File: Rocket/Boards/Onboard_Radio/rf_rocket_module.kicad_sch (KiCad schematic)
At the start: 9 parts

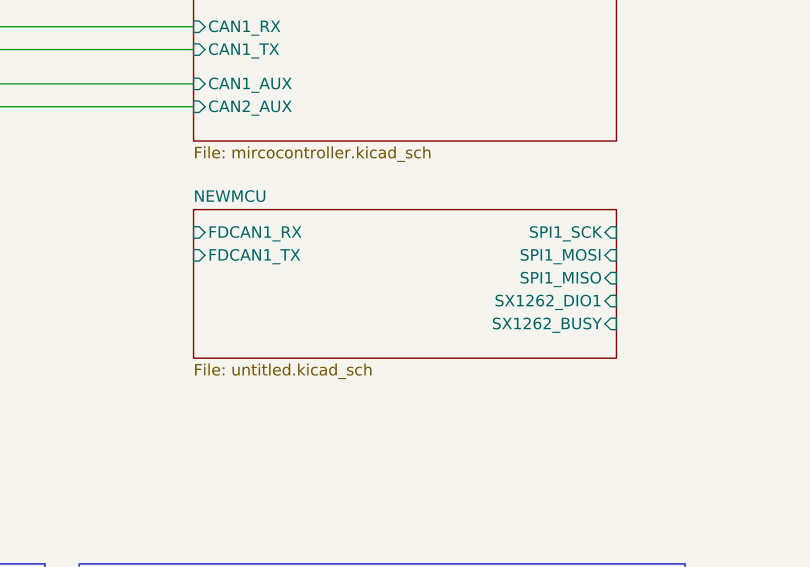
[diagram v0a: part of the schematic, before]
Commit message: python sim code added
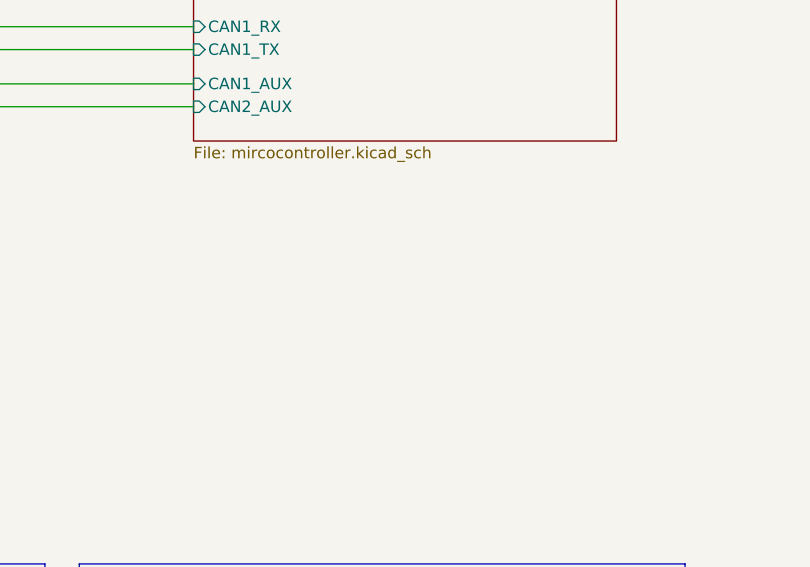
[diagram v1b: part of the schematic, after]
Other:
- removed sheet NEWMCU
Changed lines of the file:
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@@
-	)
-	(sheet
-		(at 77.47 102.87)
-		(size 46.99 16.51)
-		(exclude_from_sim no)
-		(in_bom yes)
-		(on_board yes)
-		(dnp no)
-		(fields_autoplaced yes)
-		(stroke
-			(width 0.1524)
-			(type solid)
-		)
-		(fill
-			(color 0 0 0 0.0000)
-		)
-		(property "Sheetname" "NEWMCU"
-			(at 77.47 102.1584 0)
-			(effects
-				(font
-					(size 1.27 1.27)
-				)
-				(justify left bottom)
-			)
-		)
-		(property "Sheetfile" "untitled.kicad_sch"
-			(at 77.47 119.9646 0)
-			(effects
-				(font
-					(size 1.27 1.27)
-				)
-				(justify left top)
-			)
-		)
-		(property "Field2" ""
-			(at 77.47 102.87 0)
-			(effects
-				(font
-					(size 1.27 1.27)
-				)
-			)
-		)
-		(property "Field3" ""
-			(at 77.47 102.87 0)
-			(effects
-				(font
-					(size 1.27 1.27)
-				)
-			)
-		)
-		(pin "FDCAN1_RX" input
-			(at 77.47 105.41 180)
-			(effects
-				(font
-					(size 1.27 1.27)
-				)
-				(justify left)
-			)
-		)
-		(pin "FDCAN1_TX" input
-			(at 77.47 107.95 180)
-			(effects
-				(font
-					(size 1.27 1.27)
-				)
-				(justify left)
-			)
-		)
-		(pin "SPI1_MISO" input
-			(at 124.46 110.49 0)
-			(effects
-				(font
-					(size 1.27 1.27)
-				)
-				(justify right)
-			)
-		)
-		(pin "SPI1_MOSI" input
-			(at 124.46 107.95 0)
-			(effects
-				(font
-					(size 1.27 1.27)
-				)
-				(justify right)
-			)
-		)
-		(pin "SPI1_SCK" input
-			(at 124.46 105.41 0)
-			(effects
-				(font
-					(size 1.27 1.27)
-				)
-				(justify right)
-			)
-		)
-		(pin "SX1262_BUSY" input
-			(at 124.46 115.57 0)
-			(effects
-				(font
-					(size 1.27 1.27)
-				)
-				(justify right)
-			)
-		)
-		(pin "SX1262_DIO1" input
-			(at 124.46 113.03 0)
-			(effects
-				(font
-					(size 1.27 1.27)
-				)
-				(justify right)
-			)
-		)
-		(instances
-			(project "rf_rocket_module"
-				(path "/4940ffbe-f45f-4917-a247-12e2b32b6c35"
-					(page "6")
-				)
-			)
-		)
 	)
 	(sheet

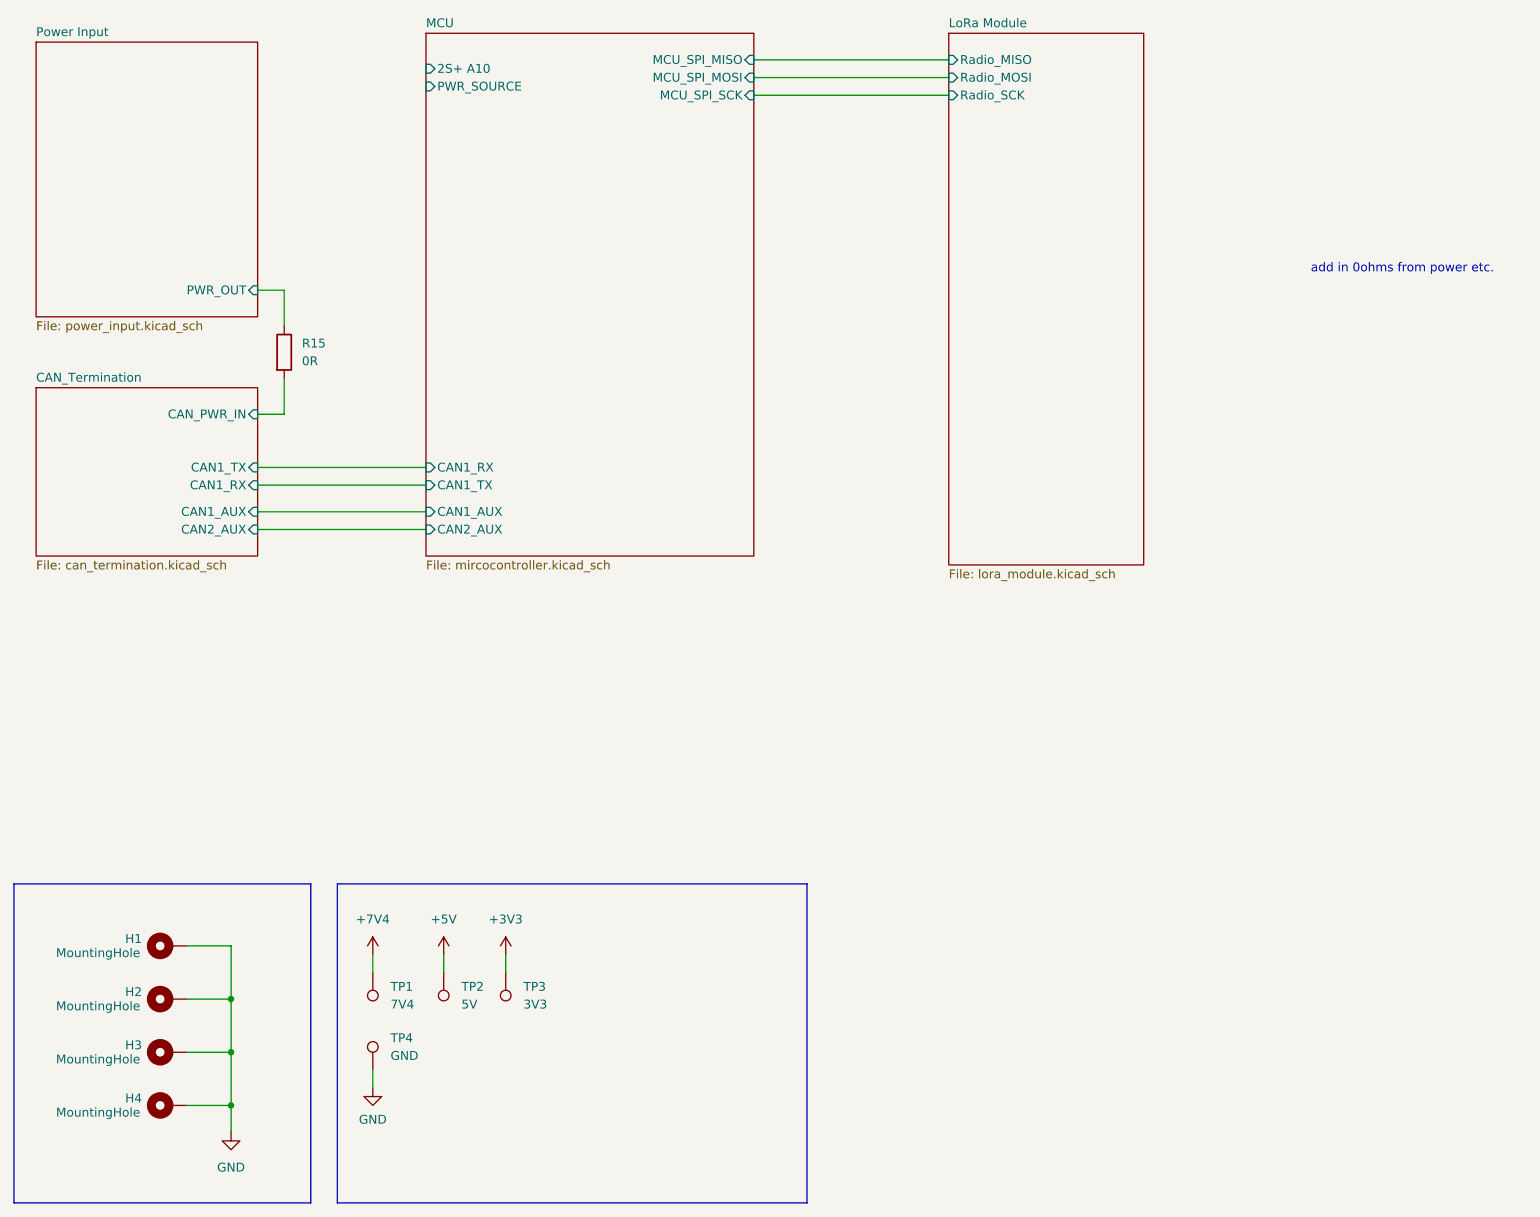
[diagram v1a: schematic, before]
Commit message: rf chip schematic changed
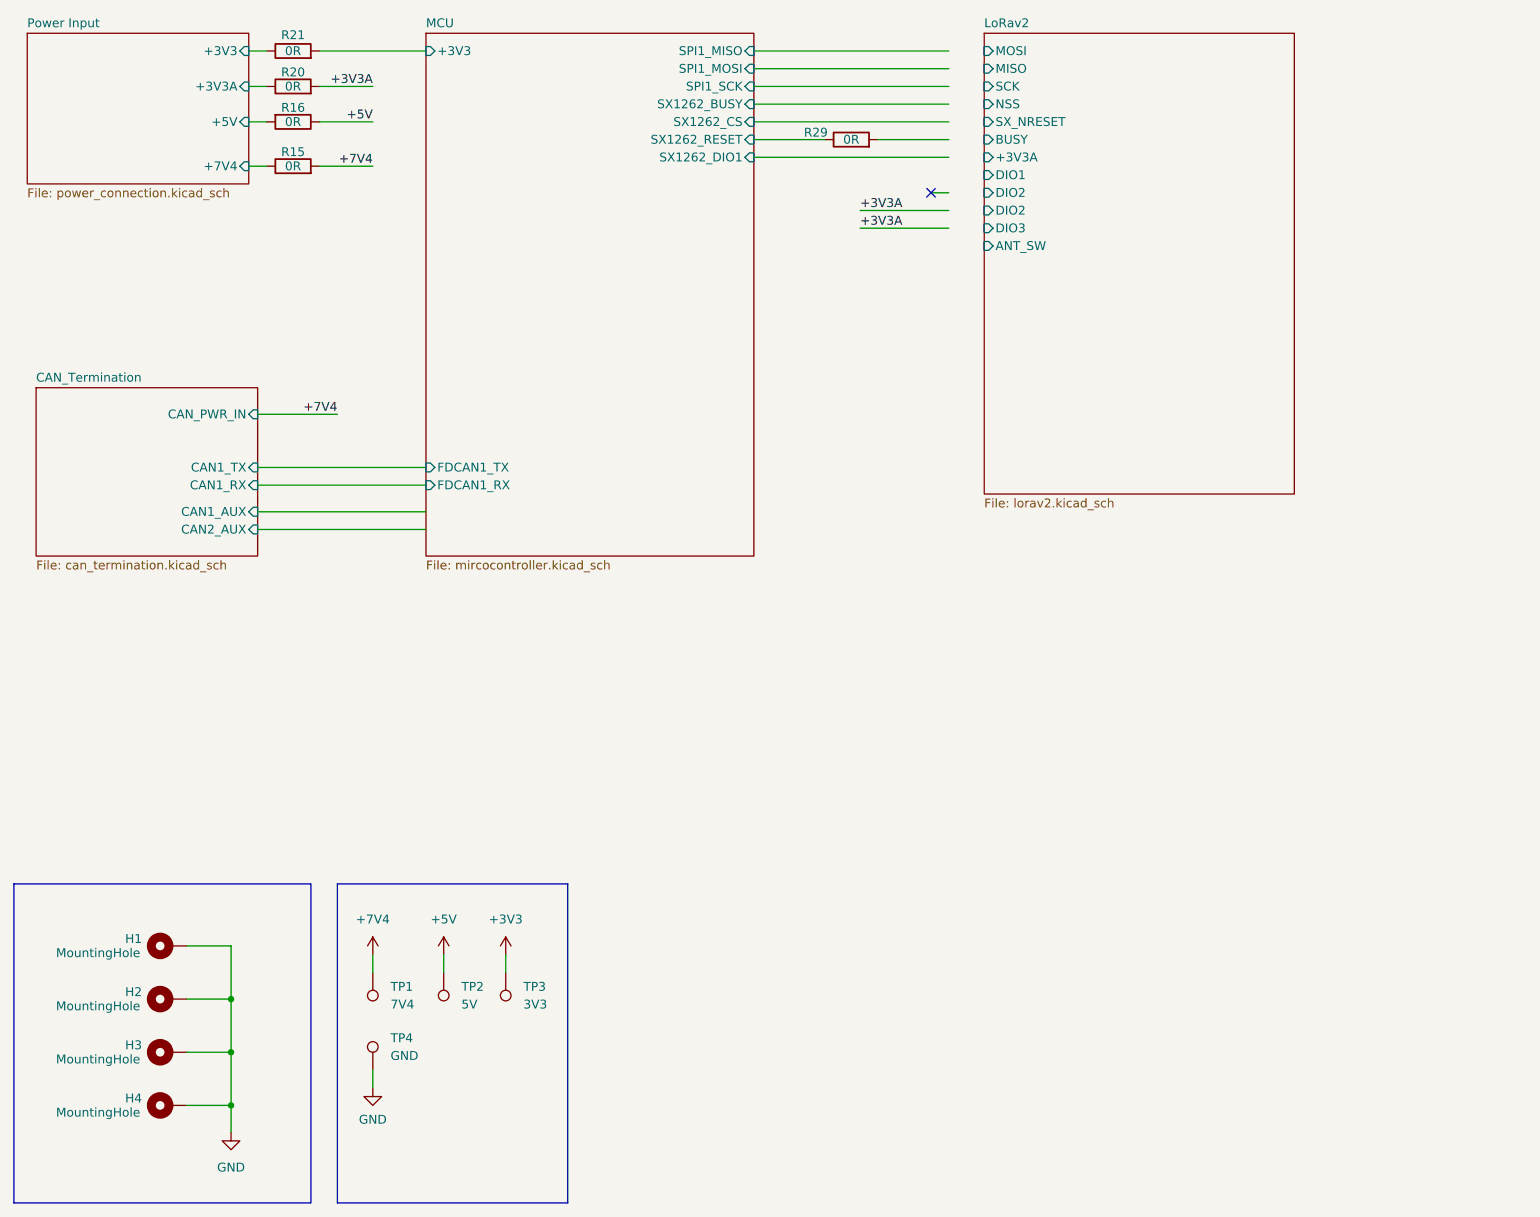
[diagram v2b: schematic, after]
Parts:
- added R16, R20, R21, R29: 0R, symbol Device:R
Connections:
- net CAN_Termination/CAN_PWR_IN is gone; now on net +7V4: R15.2
- net +5V: now also R16.1
- net Power Input/PWR_OUT renamed Power Input/+7V4
- new net +3V3A: R20.2
- new net MCU/+3V3: R21.2
- new net MCU/SX1262_RESET: R29.1
- new net Power Input/+3V3: R21.1
- new net Power Input/+3V3A: R20.1
- new net Power Input/+5V: R16.2
- no-connect marks 0 -> 1
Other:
- removed sheet LoRa Module
- added sheet LoRav2 (lorav2.kicad_sch)
- sheet MCU ports: added +3V3, FDCAN1_RX, FDCAN1_TX, SPI1_MISO, SPI1_MOSI, SPI1_SCK, SX1262_BUSY, SX1262_CS, SX1262_DIO1, SX1262_RESET; removed 2S+ A10, CAN1_AUX, CAN1_RX, CAN1_TX, CAN2_AUX, MCU_SPI_MISO, MCU_SPI_MOSI, MCU_SPI_SCK, PWR_SOURCE
- sheet Power Input: file power_input.kicad_sch -> power_connection.kicad_sch
- sheet Power Input ports: added +3V3, +3V3A, +5V, +7V4; removed PWR_OUT
- note removed: "add in 0ohms from power etc."
- moved on the sheet: R15
